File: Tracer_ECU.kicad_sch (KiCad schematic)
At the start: 173 parts, among them IC1 R5F572TFADFP#30, IC2 MPU-6500, IC3 DRV8320HRTVR, IC4 DRV8320HRTVR, IC5 DRV8320HRTVR, J1 BAT, J10 ENC2, J11 SENS2, J13 SDC, J14 ENC3, J2 DBG, J3 SENS1, J4 MOT3, J5 MOT1, J6 LIGHIT, J8 MOT2, J9 ENC1, Q1 TJ60S04M3L, Q10 FDS6898A, Q11 FDS6898A, Q12 FDS6898A, Q2 FDS6898A, Q3 FDS6898A, Q4 FDS6898A, Q6 IRLML6344TRPBF, Q7 FDS6898A, Q8 FDS6898A, Q9 FDS6898A, SW1 SW_SPDT, SW2 SW_Push, SW4 SW_Push, SW5 SW_Push, U1 NJM2732, U2 AZ1117-3.3, Y1 CSTNE20M

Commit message: アートワーク修正中． デバッグコネクタ周辺抵抗を1005M*4抵抗アレイに変更．
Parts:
- removed R1, R14, R54, R55, R56, R57, R58, R9: 4.7k, Resistor_SMD:R_0603_1608Metric_Pad0.98x0.95mm_HandSolder, symbol Device:R
- removed R40, R41, R42, R43, R70, R71, R72, R73: 470F, Resistor_SMD:R_0603_1608Metric_Pad0.98x0.95mm_HandSolder, symbol Device:R
- added JP10, JP9: Jumper, Jumper:SolderJumper-3_P1.3mm_Open_Pad1.0x1.5mm, symbol Jumper:SolderJumper_3_Open
- added JP11, JP12, JP13, JP14, JP15, JP16, JP17, JP18: Jumper, Jumper:SolderJumper-2_P1.3mm_Open_Pad1.0x1.5mm, symbol Jumper:SolderJumper_2_Open
- added R22, R23, R32, R33, R34, R35, R36, R37: 1kF, Resistor_SMD:R_0603_1608Metric_Pad0.98x0.95mm_HandSolder, symbol Device:R
- added RN1, RN2: 4.7k, My_Footprint_Lib:R_Array_Convex_4x0402, symbol Device:R_Pack04_Split
- C22, C23, C30, C31, C43: value 1000p -> 0.1u
- C29, R38: now not fitted
- JP1, JP2, JP3, JP4, JP6, JP8: footprint Jumper:SolderJumper-3_P1.3mm_Open_RoundedPad1.0x1.5mm -> Jumper:SolderJumper-3_P1.3mm_Open_Pad1.0x1.5mm
- JP5: footprint Jumper:SolderJumper-2_P1.3mm_Open_RoundedPad1.0x1.5mm -> Jumper:SolderJumper-2_P1.3mm_Bridged_Pad1.0x1.5mm
- JP7: footprint Jumper:SolderJumper-2_P1.3mm_Open_RoundedPad1.0x1.5mm -> Jumper:SolderJumper-2_P1.3mm_Open_Pad1.0x1.5mm
- R24, R25, R26, R27: value 470F -> 1kF
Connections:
- net AN000: now also R24.1; no longer R25.2, R27.2
- net AN001: now also R22.1; no longer R24.2, R26.2
- net AN002: now also R36.1
- net AN100: now also R32.1
- net AN101: now also R26.1
- net AN102: now also R34.1
- net EMLE: now also RN2.4 (R4.1)
- net GND: now also JP11.2 (B), JP12.2 (B), JP13.2 (B), JP14.2 (B), JP15.2 (B), JP16.2 (B), JP17.2 (B), JP18.2 (B), RN2.8 (R1.2); no longer C22.2, C23.2, C30.2, C31.2, C43.2, C44.2, IC1.86 (PH4/PGAVSS1), IC1.91 (PH0/PGAVSS0)
- net MD: now also RN2.3 (R3.1)
- net Mot.1_SLB: now also R24.2; no longer R27.1
- net Mot.1_SLC: now also R22.2; no longer R26.1
- net Mot.2_SLB: now also R32.2
- net Mot.2_SLC: now also R26.2
- net TCK: now also RN1.6 (R3.2)
- net TDI/RXD1: now also RN1.7 (R2.2)
- net TDO/TXD1: now also RN1.5 (R4.2)
- net TMS: now also RN1.8 (R1.2)
- net TRST#: now also RN2.1 (R1.1)
- net VCC: now also RN1.1 (R1.1), RN1.2 (R2.1), RN1.3 (R3.1), RN1.4 (R4.1), RN2.7 (R2.2)
- net at J2.7 (Pin_7), R6.1, SW2.2: now also RN2.2 (R2.1)
- net at JP1.2 (C): now also RN2.6 (R3.2)
- net at JP4.2 (C): now also R34.2
- net at JP2.2 (C): now also R36.2
- net at JP6.2 (C): now also RN2.5 (R4.2)
- net M1_RU+ renamed Mot.1_Ru+
- net Mot.1_Ru+: now also JP4.3 (B); no longer JP2.3 (B)
- net M2_RU+ renamed Mot.2_Ru+
- net Mot.2_Ru+: now also JP2.3 (B); no longer JP4.3 (B)
- new net: JP14.1 (A), R27.2
- new net: JP10.1 (A), JP17.1 (A)
- new net: JP9.2 (C), R35.2
- new net: JP10.2 (C), R37.2
- new net: JP16.1 (A), R23.2
- new net: JP18.1 (A), JP9.1 (A)
- new net: JP15.1 (A), R25.2
- new net: JP13.1 (A), R33.2
- new net Mot.1_Ru-: JP11.1 (A), JP9.3 (B)
- new net Mot.2_Ru-: JP10.3 (B), JP12.1 (A)
- new net PGAVSS0: C22.2, C23.2, C44.2, IC1.91 (PH0/PGAVSS0), R23.1, R25.1, R37.1
- new net PGAVSS1: C30.2, C31.2, C43.2, IC1.86 (PH4/PGAVSS1), R27.1, R33.1, R35.1
- now unconnected: JP3.2 (C)
- no-connect marks 11 -> 12
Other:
- moved on the sheet: C22, C23, C30, C31, C43, C44, JP2, JP4, R74, R75

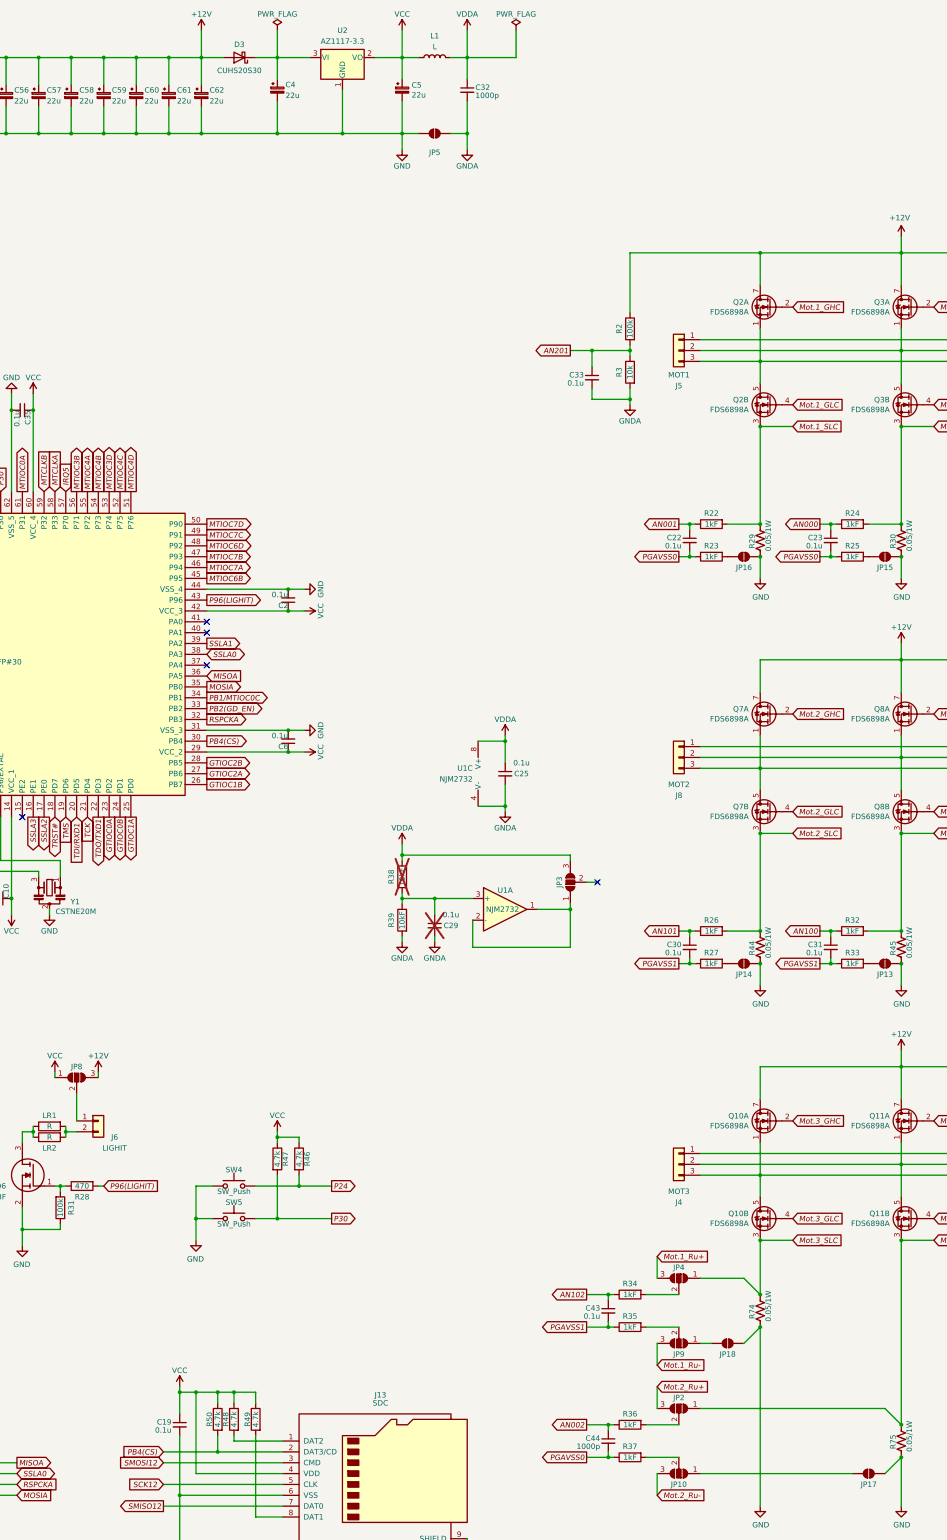
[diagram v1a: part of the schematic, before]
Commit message: DCバイアスを考慮しパワーＣサイズを変更． アートワーク修正中．
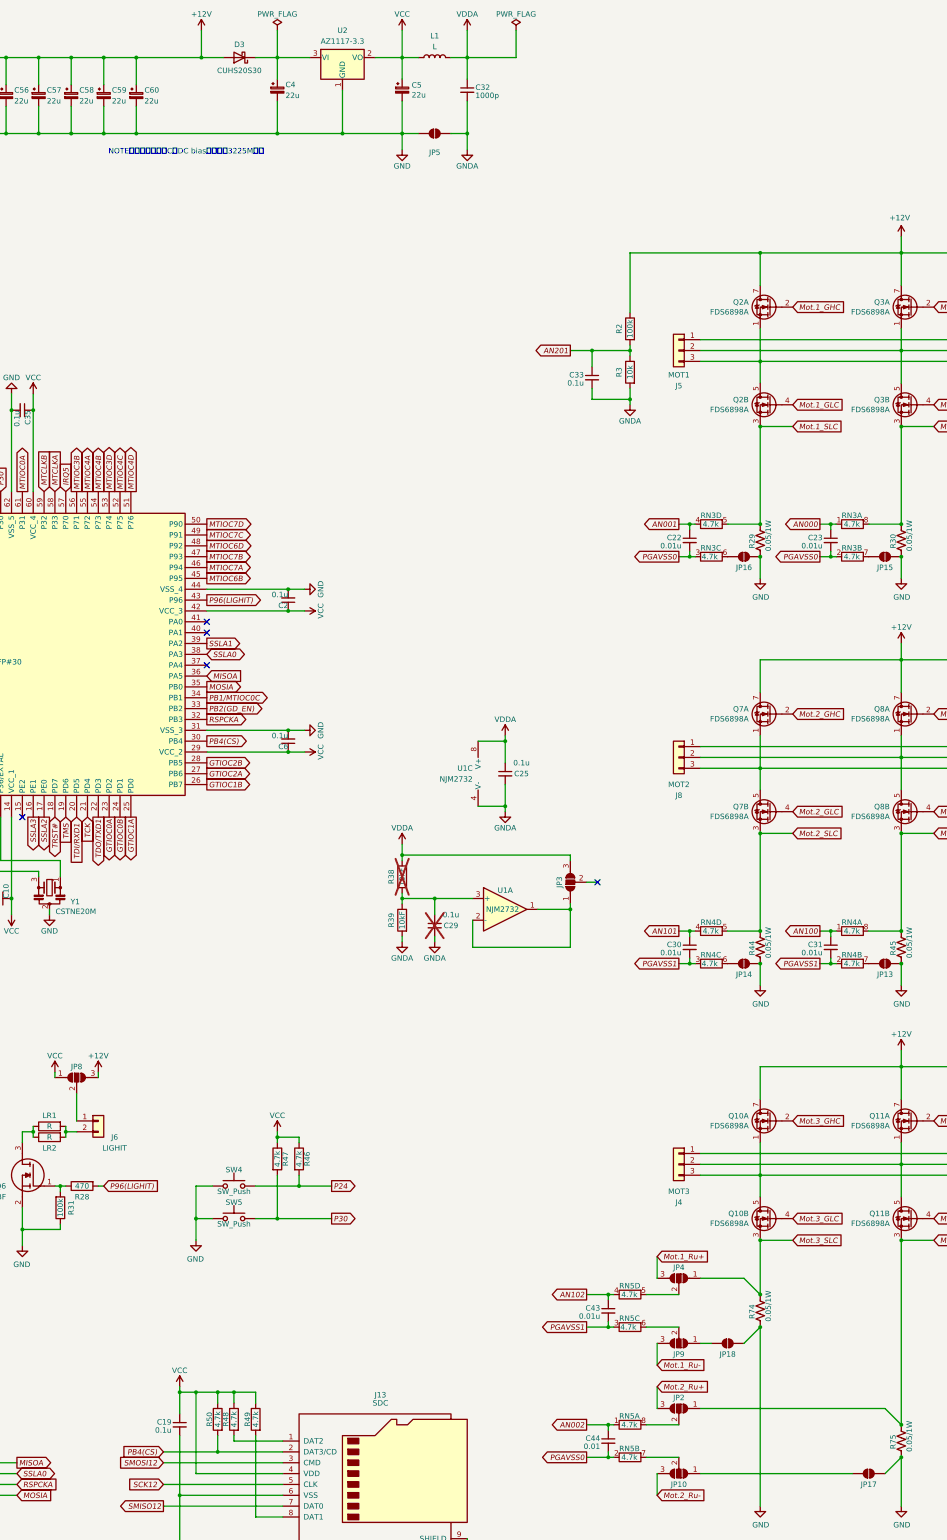
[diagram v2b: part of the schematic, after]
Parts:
- removed C61, C62: 22u, Capacitor_SMD:C_0805_2012Metric_Pad1.18x1.45mm_HandSolder, symbol Tracer_2.0-rescue:CP_Small-Device
- removed R22, R23, R24, R25, R26, R27, R32, R33, R34, R35, R36, R37: 1kF, Resistor_SMD:R_0603_1608Metric_Pad0.98x0.95mm_HandSolder, symbol Device:R
- added RN3, RN4, RN5: 4.7k, My_Footprint_Lib:R_Array_Convex_4x0402, symbol Device:R_Pack04_Split
- C22, C23, C30, C31, C43: value 0.1u -> 0.01u
- C3, C34, C36, C4, C45, C46, C47, C48, C49, C5, C50, C51, C52, C53, C55, C56, C57, C58, C59, C60: footprint Capacitor_SMD:C_0805_2012Metric_Pad1.18x1.45mm_HandSolder -> Capacitor_SMD:C_1210_3225Metric_Pad1.33x2.70mm_HandSolder
- C44: value 1000p -> 0.01
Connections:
- net AN000: now also RN3.1 (R1.1)
- net AN001: now also RN3.4 (R4.1)
- net AN002: now also RN5.1 (R1.1)
- net AN100: now also RN4.1 (R1.1)
- net AN101: now also RN4.4 (R4.1)
- net AN102: now also RN5.4 (R4.1)
- net Mot.1_SLB: now also RN3.8 (R1.2)
- net Mot.1_SLC: now also RN3.5 (R4.2)
- net Mot.2_SLB: now also RN4.8 (R1.2)
- net Mot.2_SLC: now also RN4.5 (R4.2)
- net PGAVSS0: now also RN3.2 (R2.1), RN3.3 (R3.1), RN5.2 (R2.1)
- net PGAVSS1: now also RN4.2 (R2.1), RN4.3 (R3.1), RN5.3 (R3.1)
- net at JP14.1 (A): now also RN4.6 (R3.2)
- net at JP9.2 (C): now also RN5.6 (R3.2)
- net at JP10.2 (C): now also RN5.7 (R2.2)
- net at JP2.2 (C): now also RN5.8 (R1.2)
- net at JP16.1 (A): now also RN3.6 (R3.2)
- net at JP15.1 (A): now also RN3.7 (R2.2)
- net at JP4.2 (C): now also RN5.5 (R4.2)
- net at JP13.1 (A): now also RN4.7 (R2.2)
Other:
- note added: "NOTE：パワーラインCはDC biasを考慮し3225M以上"
